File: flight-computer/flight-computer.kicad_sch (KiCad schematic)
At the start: 49 parts, among them J1 MicroSD Slot, J2 USB_C_Receptacle_USB2.0_16P, Q2 NMOS, SW1 SW_Push, SW2 SW_Push, U1 RP2040, U2 W25Q16JVSS, U3 USBLC6-2SC6, Y1 12MHz

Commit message: Remove out of stock LED from BOMS
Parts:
- D2, D3: MP LG R971-KN-1 -> HSMG-C170
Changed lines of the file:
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@@
 			)
 		)
-		(property "Datasheet" "https://www.mouser.ca/datasheet/2/588/prd_pim_datasheet_2191277_EN_pdf-3419125.pdf"
+		(property "Datasheet" ""
 			(at 264.16 224.79 0)
 			(effects
@@
 			)
 		)
-		(property "MP" "LG R971-KN-1"
+		(property "MP" "HSMG-C170"
 			(at 264.16 224.79 0)
 			(effects
@@
 			)
 		)
-		(property "Datasheet" "https://www.mouser.ca/datasheet/2/588/prd_pim_datasheet_2191277_EN_pdf-3419125.pdf"
+		(property "Datasheet" ""
 			(at 204.47 224.79 0)
 			(effects
@@
 			)
 		)
-		(property "MP" "LG R971-KN-1"
+		(property "MP" "HSMG-C170"
 			(at 204.47 224.79 0)
 			(effects

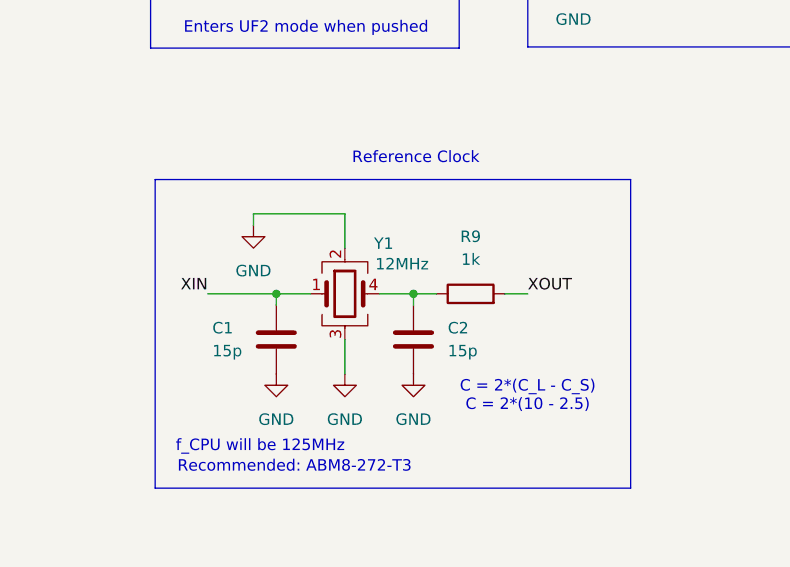
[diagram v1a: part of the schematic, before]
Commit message: Updated to REV-B; KiCAD's default footprint (or at least first appearing) for the SMD crystal didn't match the datasheet and I didn't catch that. This was the only thing preventing me from booting an otherwise good board. Always check your footprints against the datasheet.
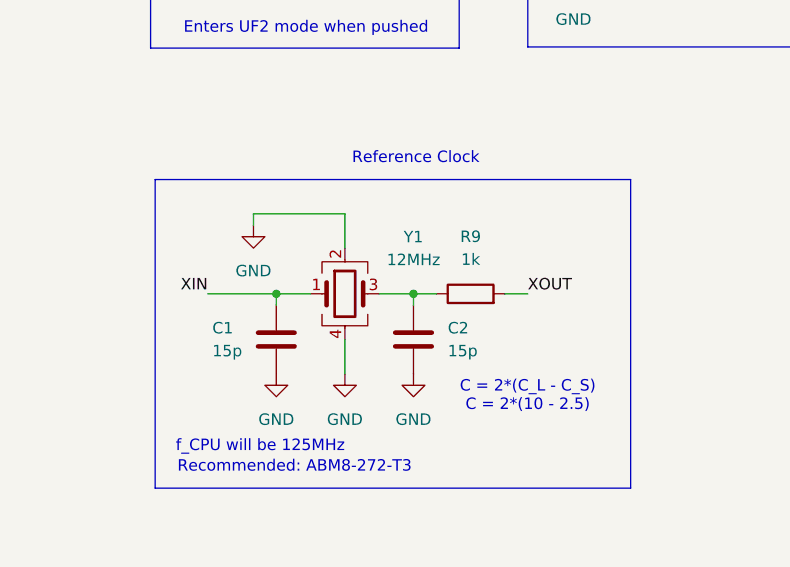
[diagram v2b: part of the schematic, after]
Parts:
- removed Y1: 12MHz, Crystal:Crystal_SMD_3225-4Pin_3.2x2.5mm, symbol Device:Crystal_GND23
- added Y1: 12MHz, Crystal:Crystal_SMD_3225-4Pin_3.2x2.5mm, symbol Device:Crystal_GND24
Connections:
- net GND: now also Y1.2, Y1.4
- net XIN: now also Y1.1
- net at C2.1, R9.1: now also Y1.3
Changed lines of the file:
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@@
 		(title "Pygmy")
 		(date "2024-11-10")
-		(rev "A")
+		(rev "B")
 		(company "Matteo Golin")
 		(comment 1 "Use JLC04161H-7628")
@@
 	)
 	(symbol
-		(lib_id "Device:Crystal_GND23")
+		(lib_id "Device:Crystal_GND24")
 		(at 55.88 77.47 0)
 		(unit 1)
@@
 		(on_board yes)
 		(dnp no)
+		(fields_autoplaced yes)
 		(property "Reference" "Y1"
-			(at 60.198 71.882 0)
+			(at 63.5 71.1514 0)
 			(effects
 				(font
@@
 		)
 		(property "Value" "12MHz"
-			(at 62.23 74.168 0)
+			(at 63.5 73.6914 0)
 			(effects
 				(font
@@
 			)
 		)
-		(property "Datasheet" "https://abracon.com/datasheets/ABM8-272-T3.pdf"
+		(property "Datasheet" "https://www.mouser.ca/datasheet/2/3/ABM8_272_T3-3392615.pdf"
 			(at 55.88 77.47 0)
 			(effects
@@
 			)
 		)
-		(property "Description" "Four pin crystal, GND on pins 2 and 3"
+		(property "Description" "Four pin crystal, GND on pins 2 and 4"
 			(at 55.88 77.47 0)
 			(effects
@@
 			)
 		)
-		(property "MP" "ABM8-272-T3"
-			(at 55.88 77.47 0)
-			(effects
-				(font
-					(size 1.27 1.27)
-				)
-				(hide yes)
-			)
+		(pin "2"
+		)
+		(pin "1"
 		)
 		(pin "4"
@@
 		(pin "3"
 		)
-		(pin "2"
-		)
-		(pin "1"
-		)
 		(instances
